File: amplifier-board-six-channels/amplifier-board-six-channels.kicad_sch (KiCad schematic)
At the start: 9 parts, among them J1 Conn_02x08_Odd_Even, J2 Conn_02x08_Odd_Even, U7 MAX6035xxUR25

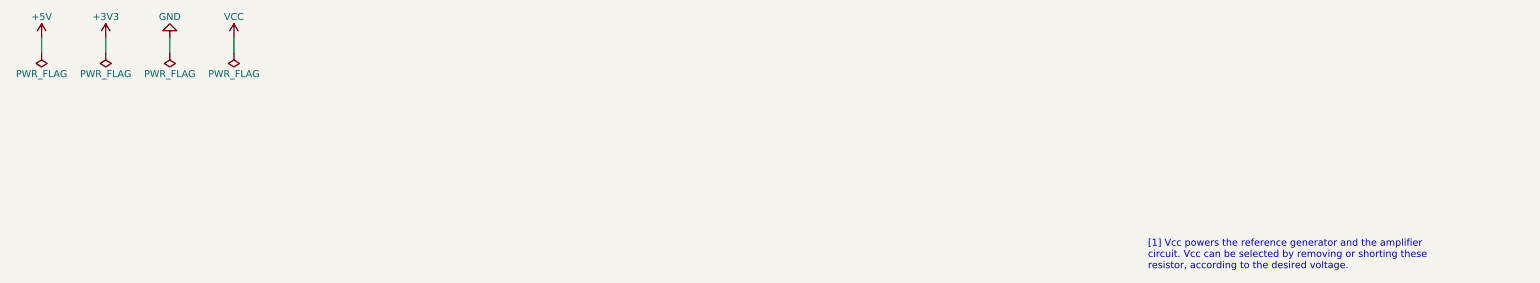
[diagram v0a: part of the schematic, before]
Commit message: Generated gerber files for amplifier board
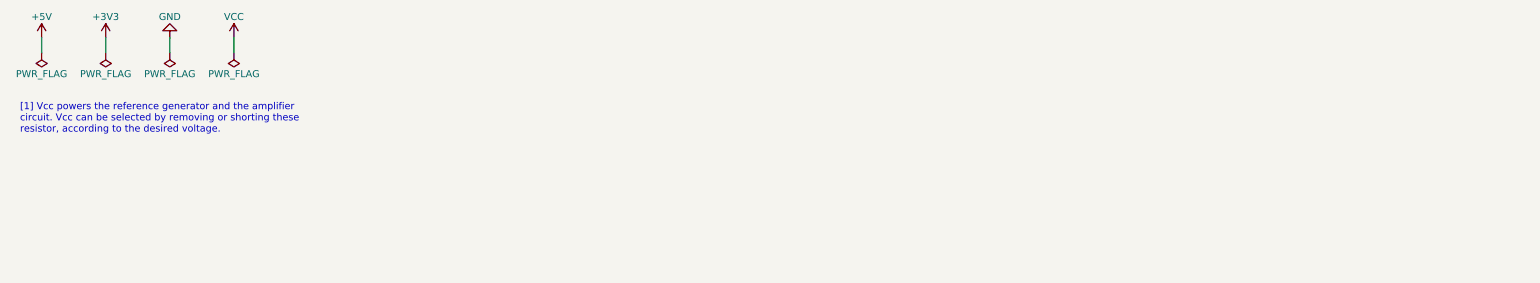
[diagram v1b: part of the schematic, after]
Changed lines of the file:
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@@
   )
   (text "[1] Vcc powers the reference generator and the amplifier \ncircuit. Vcc can be selected by removing or shorting these\nresistor, according to the desired voltage."
-    (at 224.028 128.27 0)
+    (at 18.415 103.378 0)
     (effects (font (size 1.27 1.27)) (justify left bottom))
   )

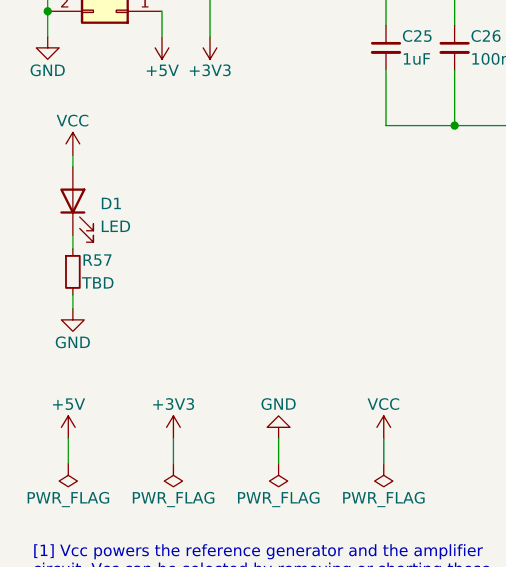
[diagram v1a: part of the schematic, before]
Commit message: Updated gain values and created bom for amplifier board
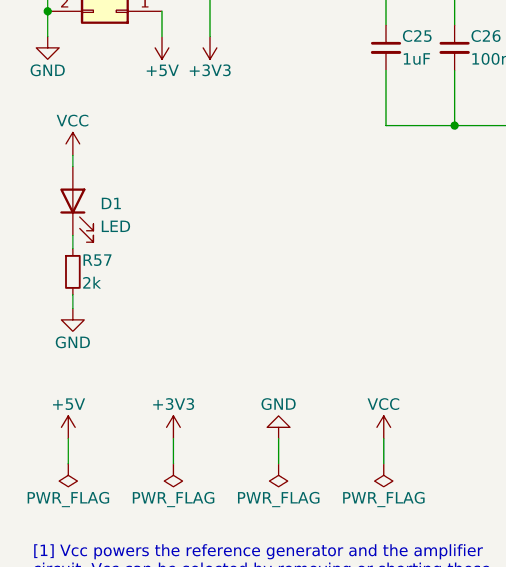
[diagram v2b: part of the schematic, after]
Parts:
- R57: value TBD -> 2k
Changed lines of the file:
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@@
       (effects (font (size 1.27 1.27)) (justify left))
     )
-    (property "Value" "TBD" (id 1) (at 23.876 68.58 0)
+    (property "Value" "2k" (id 1) (at 23.876 68.58 0)
       (effects (font (size 1.27 1.27)) (justify left))
     )
@@
     )
     (path "/4efaab83-6808-4db3-9e3e-81e3bce3a6f7/e4148d4d-dadf-4cd1-aff5-da527cd2ba60"
-      (reference "R3") (unit 1) (value "TBD") (footprint "Resistor_SMD:R_0805_2012Metric")
+      (reference "R3") (unit 1) (value "22k") (footprint "Resistor_SMD:R_0805_2012Metric")
     )
     (path "/4efaab83-6808-4db3-9e3e-81e3bce3a6f7/400a5b14-85a2-4958-95ad-a704d3c0136a"
@@
     )
     (path "/4efaab83-6808-4db3-9e3e-81e3bce3a6f7/0951b021-850c-411f-9fee-879752d2b3e9"
-      (reference "R7") (unit 1) (value "TBD") (footprint "Resistor_SMD:R_0805_2012Metric")
+      (reference "R7") (unit 1) (value "22k") (footprint "Resistor_SMD:R_0805_2012Metric")
     )
     (path "/4efaab83-6808-4db3-9e3e-81e3bce3a6f7/a46addc9-9332-48cc-9d1d-a2ec0d03fd56"
@@
     )
     (path "/bbf9a57d-3a72-446f-8bcd-829885a0a313/e4148d4d-dadf-4cd1-aff5-da527cd2ba60"
-      (reference "R12") (unit 1) (value "TBD") (footprint "Resistor_SMD:R_0805_2012Metric")
+      (reference "R12") (unit 1) (value "22k") (footprint "Resistor_SMD:R_0805_2012Metric")
     )
     (path "/bbf9a57d-3a72-446f-8bcd-829885a0a313/400a5b14-85a2-4958-95ad-a704d3c0136a"
@@
     )
     (path "/bbf9a57d-3a72-446f-8bcd-829885a0a313/0951b021-850c-411f-9fee-879752d2b3e9"
-      (reference "R16") (unit 1) (value "TBD") (footprint "Resistor_SMD:R_0805_2012Metric")
+      (reference "R16") (unit 1) (value "22k") (footprint "Resistor_SMD:R_0805_2012Metric")
     )
     (path "/bbf9a57d-3a72-446f-8bcd-829885a0a313/a46addc9-9332-48cc-9d1d-a2ec0d03fd56"
@@
     )
     (path "/09f7c8dd-2a3f-4fed-bd01-bb86fdc40eaf/e4148d4d-dadf-4cd1-aff5-da527cd2ba60"
-      (reference "R21") (unit 1) (value "TBD") (footprint "Resistor_SMD:R_0805_2012Metric")
+      (reference "R21") (unit 1) (value "22k") (footprint "Resistor_SMD:R_0805_2012Metric")
     )
     (path "/09f7c8dd-2a3f-4fed-bd01-bb86fdc40eaf/400a5b14-85a2-4958-95ad-a704d3c0136a"
@@
     )
     (path "/09f7c8dd-2a3f-4fed-bd01-bb86fdc40eaf/0951b021-850c-411f-9fee-879752d2b3e9"
-      (reference "R25") (unit 1) (value "TBD") (footprint "Resistor_SMD:R_0805_2012Metric")
+      (reference "R25") (unit 1) (value "22k") (footprint "Resistor_SMD:R_0805_2012Metric")
     )
     (path "/09f7c8dd-2a3f-4fed-bd01-bb86fdc40eaf/a46addc9-9332-48cc-9d1d-a2ec0d03fd56"
@@
     )
     (path "/bba7da7b-d30a-49e0-8864-383547d8467f/e4148d4d-dadf-4cd1-aff5-da527cd2ba60"
-      (reference "R30") (unit 1) (value "TBD") (footprint "Resistor_SMD:R_0805_2012Metric")
+      (reference "R30") (unit 1) (value "22k") (footprint "Resistor_SMD:R_0805_2012Metric")
     )
     (path "/bba7da7b-d30a-49e0-8864-383547d8467f/400a5b14-85a2-4958-95ad-a704d3c0136a"
@@
     )
     (path "/bba7da7b-d30a-49e0-8864-383547d8467f/0951b021-850c-411f-9fee-879752d2b3e9"
-      (reference "R34") (unit 1) (value "TBD") (footprint "Resistor_SMD:R_0805_2012Metric")
+      (reference "R34") (unit 1) (value "22k") (footprint "Resistor_SMD:R_0805_2012Metric")
     )
     (path "/bba7da7b-d30a-49e0-8864-383547d8467f/a46addc9-9332-48cc-9d1d-a2ec0d03fd56"
@@
     )
     (path "/8ab19342-0ecc-429d-852f-291b06965637/e4148d4d-dadf-4cd1-aff5-da527cd2ba60"
-      (reference "R39") (unit 1) (value "TBD") (footprint "Resistor_SMD:R_0805_2012Metric")
+      (reference "R39") (unit 1) (value "22k") (footprint "Resistor_SMD:R_0805_2012Metric")
     )
     (path "/8ab19342-0ecc-429d-852f-291b06965637/400a5b14-85a2-4958-95ad-a704d3c0136a"
@@
     )
     (path "/8ab19342-0ecc-429d-852f-291b06965637/0951b021-850c-411f-9fee-879752d2b3e9"
-      (reference "R43") (unit 1) (value "TBD") (footprint "Resistor_SMD:R_0805_2012Metric")
+      (reference "R43") (unit 1) (value "22k") (footprint "Resistor_SMD:R_0805_2012Metric")
     )
     (path "/8ab19342-0ecc-429d-852f-291b06965637/a46addc9-9332-48cc-9d1d-a2ec0d03fd56"
@@
     )
     (path "/584092ce-bc20-41b0-9a12-0992358c4321/e4148d4d-dadf-4cd1-aff5-da527cd2ba60"
-      (reference "R48") (unit 1) (value "TBD") (footprint "Resistor_SMD:R_0805_2012Metric")
+      (reference "R48") (unit 1) (value "22k") (footprint "Resistor_SMD:R_0805_2012Metric")
     )
     (path "/584092ce-bc20-41b0-9a12-0992358c4321/400a5b14-85a2-4958-95ad-a704d3c0136a"
@@
     )
     (path "/584092ce-bc20-41b0-9a12-0992358c4321/0951b021-850c-411f-9fee-879752d2b3e9"
-      (reference "R52") (unit 1) (value "TBD") (footprint "Resistor_SMD:R_0805_2012Metric")
+      (reference "R52") (unit 1) (value "22k") (footprint "Resistor_SMD:R_0805_2012Metric")
     )
     (path "/584092ce-bc20-41b0-9a12-0992358c4321/a46addc9-9332-48cc-9d1d-a2ec0d03fd56"
@@
     )
     (path "/a8294594-9930-4eb8-a5e5-03aa3c9bfe76"
-      (reference "R57") (unit 1) (value "TBD") (footprint "Resistor_SMD:R_0805_2012Metric")
+      (reference "R57") (unit 1) (value "2k") (footprint "Resistor_SMD:R_0805_2012Metric")
     )
     (path "/4efaab83-6808-4db3-9e3e-81e3bce3a6f7/fc86223e-1a3d-4dbf-ad80-1c2ccac1681c"
